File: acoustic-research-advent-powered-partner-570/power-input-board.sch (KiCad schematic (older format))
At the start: 12 parts, among them J24 DNP

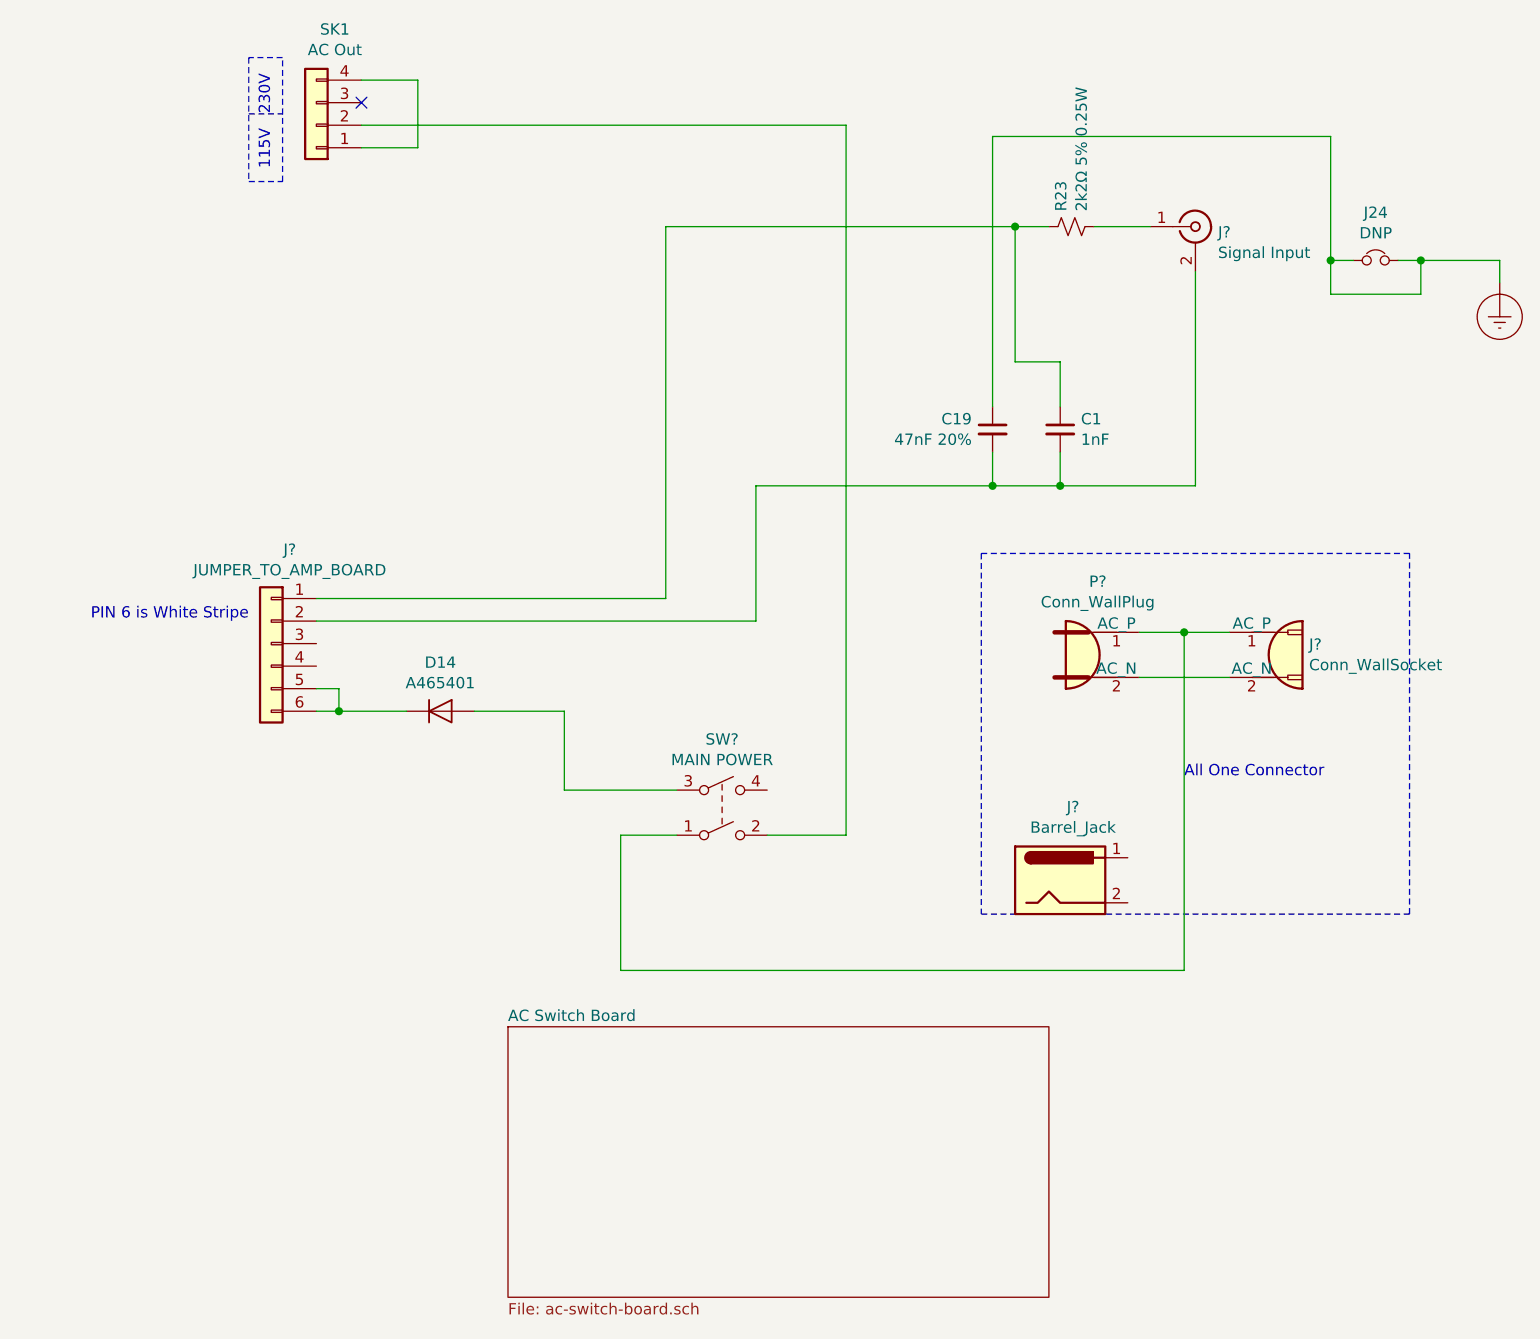
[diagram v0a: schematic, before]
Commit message: finished input board
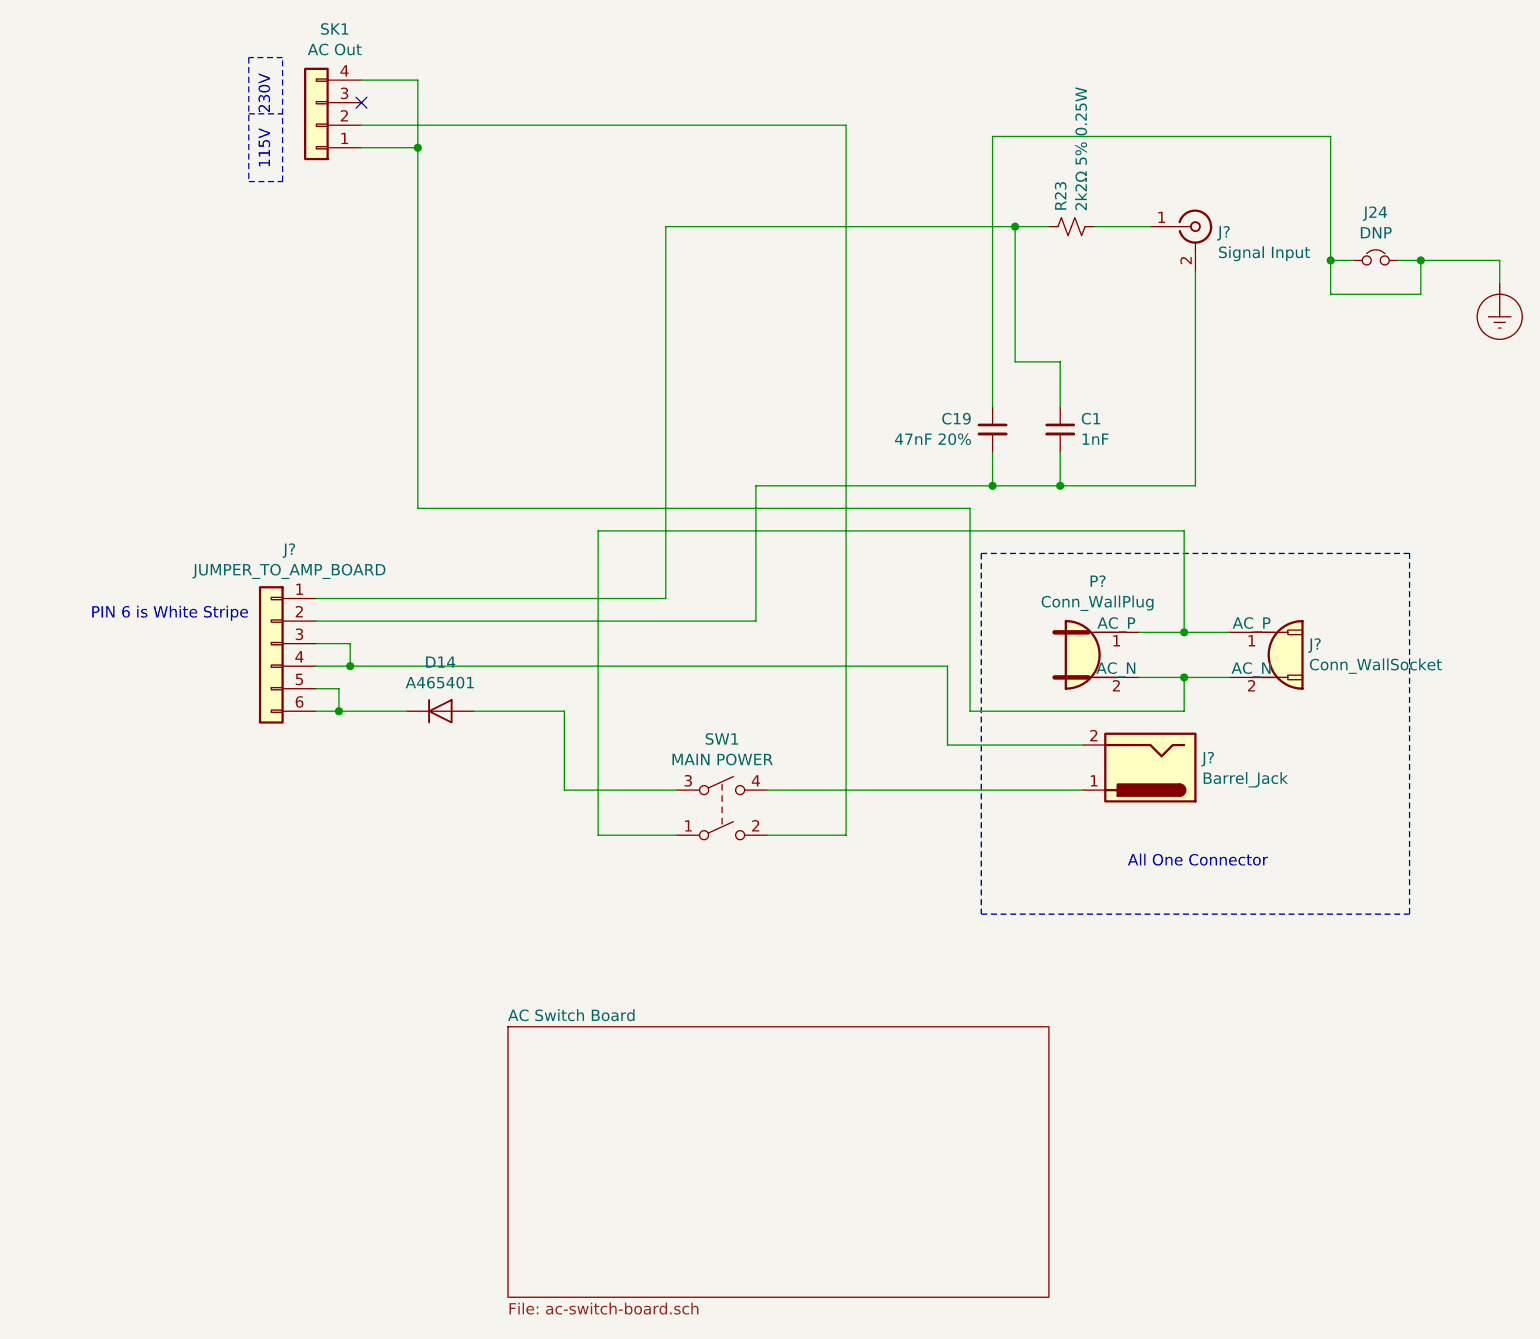
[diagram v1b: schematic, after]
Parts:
- gave numbers to parts that had none: 1
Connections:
- net at SK1.1 (Pin_1), SK1.4 (Pin_4): now also J?.2 (AC_N), P?.2 (AC_N)
- net at J?.3 (Pin_3): now also J?.2, J?.4 (Pin_4)
- net at SW1.4: now also J?.1
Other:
- moved on the sheet: J?
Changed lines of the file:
@@
 	2200 4500 2500 4500
 $Comp
-L Switch:SW_DPST SW?
+L Switch:SW_DPST SW1
 U 1 1 6581F068
 P 3900 4950
-F 0 "SW?" H 3900 5275 50  0000 C CNN
+F 0 "SW1" H 3900 5275 50  0000 C CNN
 F 1 "MAIN POWER" H 3900 5184 50  0000 C CNN
 F 2 "" H 3900 4950 50  0001 C CNN
@@
 L Connector:Barrel_Jack J?
 U 1 1 65830C1E
-P 5400 5250
+P 5800 4750
 AR Path="/5E8CC7CC/6582399F/65830C1E" Ref="J?"  Part="1"
 AR Path="/5E8CC7CC/65830C1E" Ref="J?"  Part="1"
-F 0 "J?" H 5457 5575 50  0000 C CNN
-F 1 "Barrel_Jack" H 5457 5484 50  0000 C CNN
-F 2 "" H 5450 5210 50  0001 C CNN
-F 3 "~" H 5450 5210 50  0001 C CNN
-	1    5400 5250
-	1    0    0    -1
+F 0 "J?" H 5570 4708 50  0000 R CNN
+F 1 "Barrel_Jack" H 5570 4799 50  0000 R CNN
+F 2 "" H 5850 4710 50  0001 C CNN
+F 3 "~" H 5850 4710 50  0001 C CNN
+	1    5800 4750
+	-1   0    0    1
 $EndComp
 Wire Notes Line
@@
 Wire Notes Line
 	6950 3800 5050 3800
-Text Notes 5950 4800 0    50   ~ 0
+Text Notes 5700 5200 0    50   ~ 0
 All One Connector
 Wire Wire Line
 	5750 4150 5950 4150
-Wire Wire Line
-	3700 5050 3450 5050
-Wire Wire Line
-	3450 5050 3450 5650
-Wire Wire Line
-	3450 5650 5950 5650
-Wire Wire Line
-	5950 5650 5950 4150
 Connection ~ 5950 4150
 Wire Wire Line
 	5950 4150 6150 4150
 Wire Wire Line
-	5750 4350 6150 4350
+	5750 4350 5950 4350
 $Comp
 L Connector:Conn_Coaxial J?
@@
 	3650 4000 2100 4000
 Connection ~ 5200 2350
+Wire Wire Line
+	2100 4200 2250 4200
+Wire Wire Line
+	2250 4200 2250 4300
+Wire Wire Line
+	2250 4300 2100 4300
+Wire Wire Line
+	4900 4650 4900 4300
+Wire Wire Line
+	4900 4300 2250 4300
+Connection ~ 2250 4300
+Wire Wire Line
+	4900 4650 5500 4650
+Wire Wire Line
+	5500 4850 4100 4850
+Wire Wire Line
+	5950 4150 5950 3700
+Wire Wire Line
+	5950 3700 3350 3700
+Wire Wire Line
+	3350 3700 3350 5050
+Wire Wire Line
+	3350 5050 3700 5050
+Wire Wire Line
+	5950 4350 5950 4500
+Wire Wire Line
+	5950 4500 5000 4500
+Wire Wire Line
+	5000 4500 5000 3600
+Wire Wire Line
+	5000 3600 2550 3600
+Wire Wire Line
+	2550 3600 2550 2000
+Connection ~ 5950 4350
+Wire Wire Line
+	5950 4350 6150 4350
+Connection ~ 2550 2000
 $EndSCHEMATC

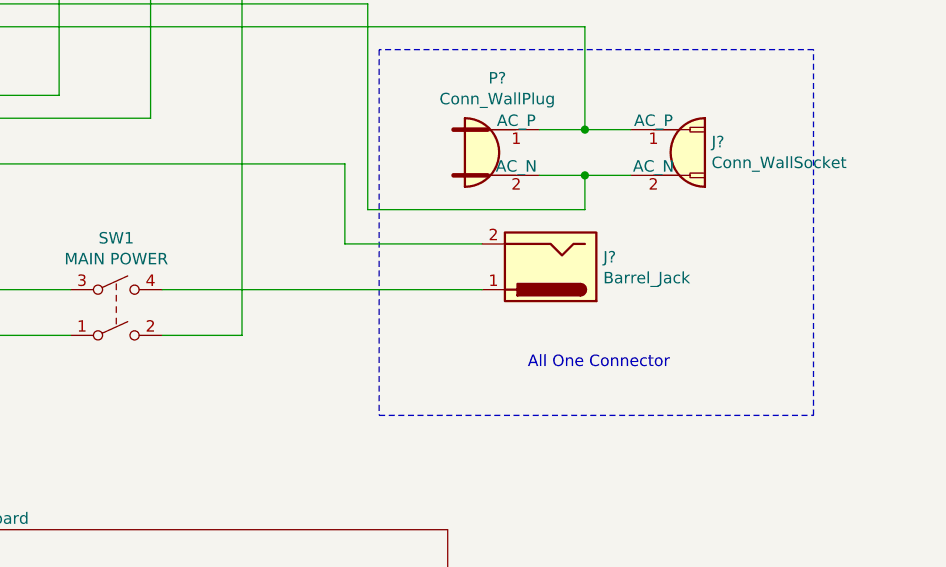
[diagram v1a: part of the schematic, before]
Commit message: added DC disconnect switch
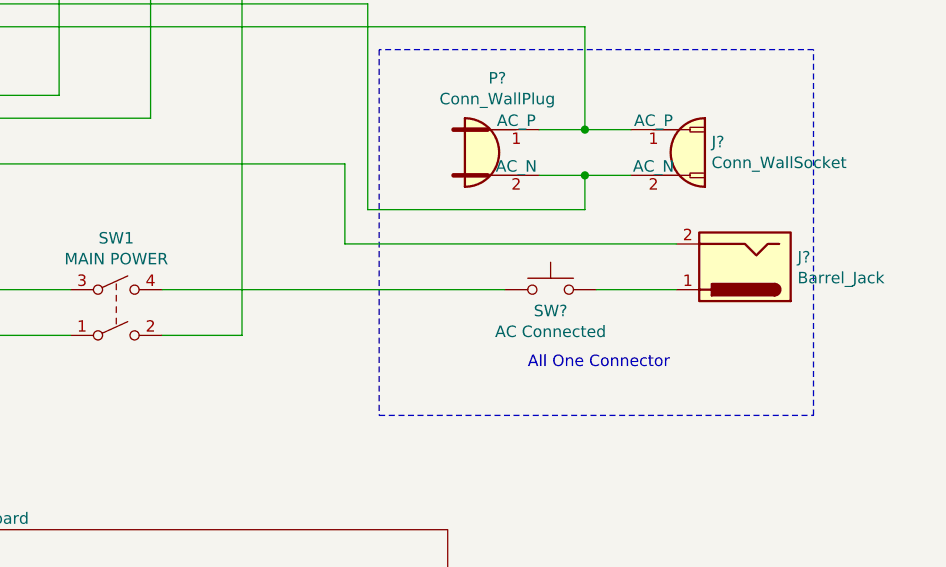
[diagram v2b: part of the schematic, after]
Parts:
- added SW?: AC Connected, symbol Switch:SW_Push
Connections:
- net at SW1.4: now also SW?.1; no longer J?.1
- new net: J?.1, SW?.2
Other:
- moved on the sheet: J?
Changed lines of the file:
@@
 L Connector:Barrel_Jack J?
 U 1 1 65830C1E
-P 5800 4750
+P 6650 4750
 AR Path="/5E8CC7CC/6582399F/65830C1E" Ref="J?"  Part="1"
 AR Path="/5E8CC7CC/65830C1E" Ref="J?"  Part="1"
-F 0 "J?" H 5570 4708 50  0000 R CNN
-F 1 "Barrel_Jack" H 5570 4799 50  0000 R CNN
-F 2 "" H 5850 4710 50  0001 C CNN
-F 3 "~" H 5850 4710 50  0001 C CNN
-	1    5800 4750
+F 0 "J?" H 6420 4708 50  0000 R CNN
+F 1 "Barrel_Jack" H 6420 4799 50  0000 R CNN
+F 2 "" H 6700 4710 50  0001 C CNN
+F 3 "~" H 6700 4710 50  0001 C CNN
+	1    6650 4750
 	-1   0    0    1
 $EndComp
@@
 Connection ~ 2250 4300
 Wire Wire Line
-	4900 4650 5500 4650
+	4900 4650 6350 4650
 Wire Wire Line
-	5500 4850 4100 4850
+	6350 4850 6000 4850
 Wire Wire Line
 	5950 4150 5950 3700
@@
 	5950 4350 6150 4350
 Connection ~ 2550 2000
+$Comp
+L Switch:SW_Push SW?
+U 1 1 65865EB1
+P 5800 4850
+F 0 "SW?" H 5800 4757 50  0000 C CNN
+F 1 "AC Connected" H 5800 4666 50  0000 C CNN
+F 2 "" H 5800 5050 50  0001 C CNN
+F 3 "~" H 5800 5050 50  0001 C CNN
+	1    5800 4850
+	1    0    0    -1
+$EndComp
+Wire Wire Line
+	5600 4850 4100 4850
 $EndSCHEMATC
